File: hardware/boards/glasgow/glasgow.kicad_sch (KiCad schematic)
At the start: 95 parts, among them J1 USB_C_USB2.0, SW1 RST, U1 CY7C68013A-56LTX, U15 TPD3S014, U2 CAT24M01X, U3 BL24C256A-SFRC, U30 ICE40HX8K-BG121, U36 TLV73312PQDRVR, U7 APX811-40UG-7, U8 TLV75533PDRVR, Y1 24M

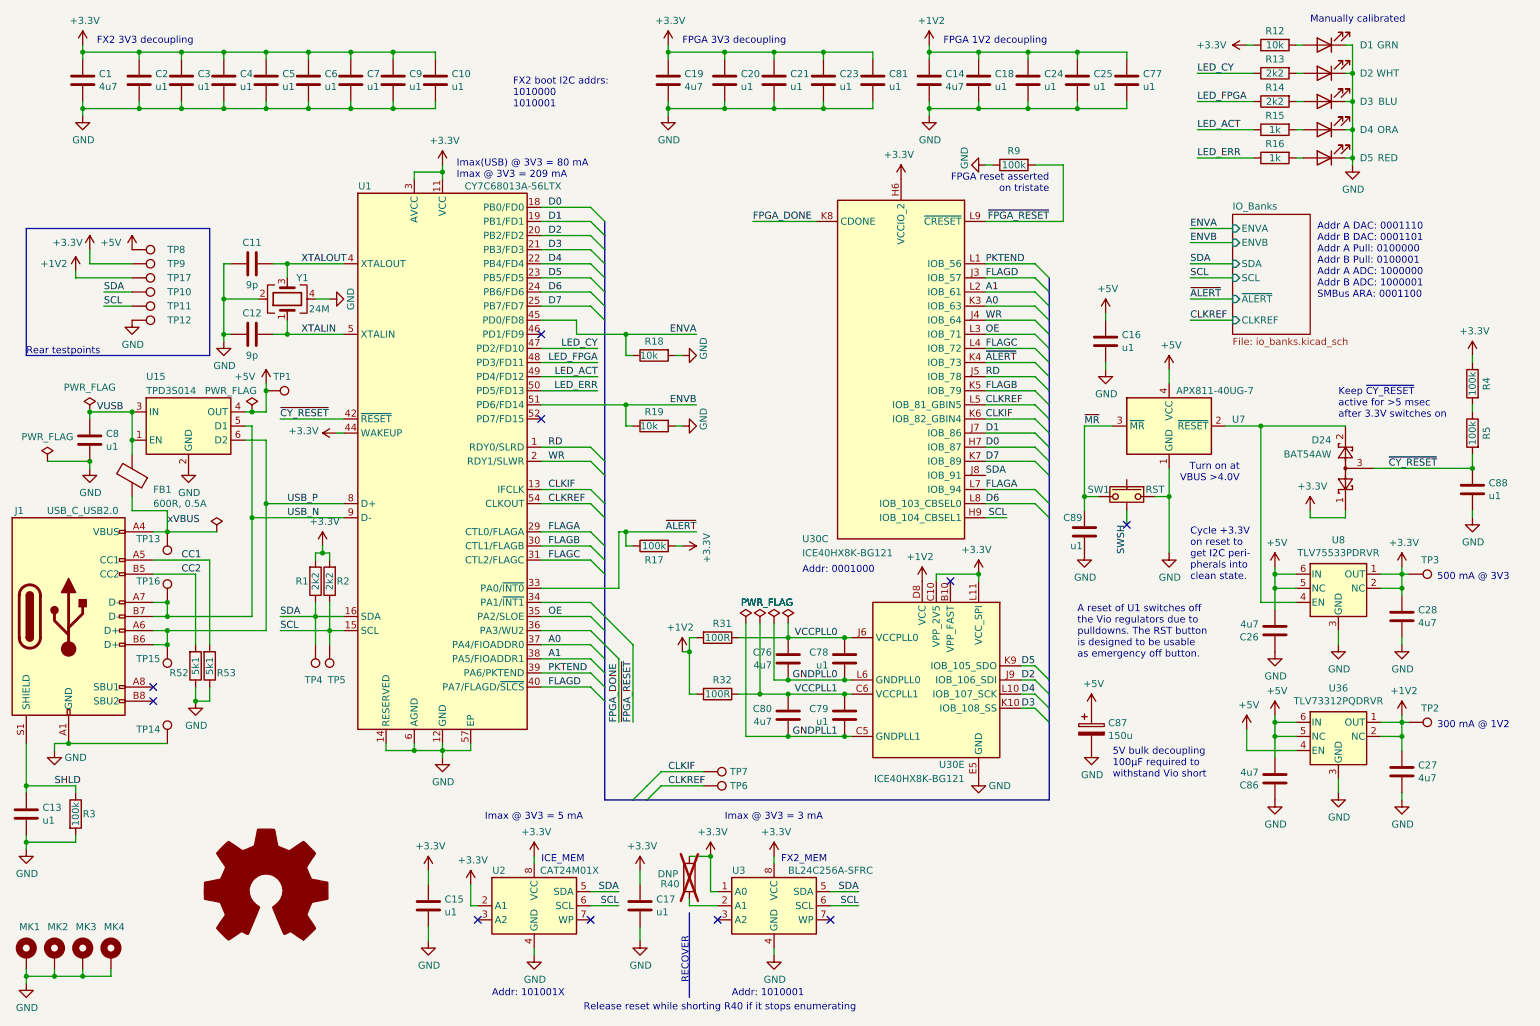
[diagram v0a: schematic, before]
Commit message: JLCPCB part swaps
Switch parts to be either of:
- cheaper
- in stock
- order-able
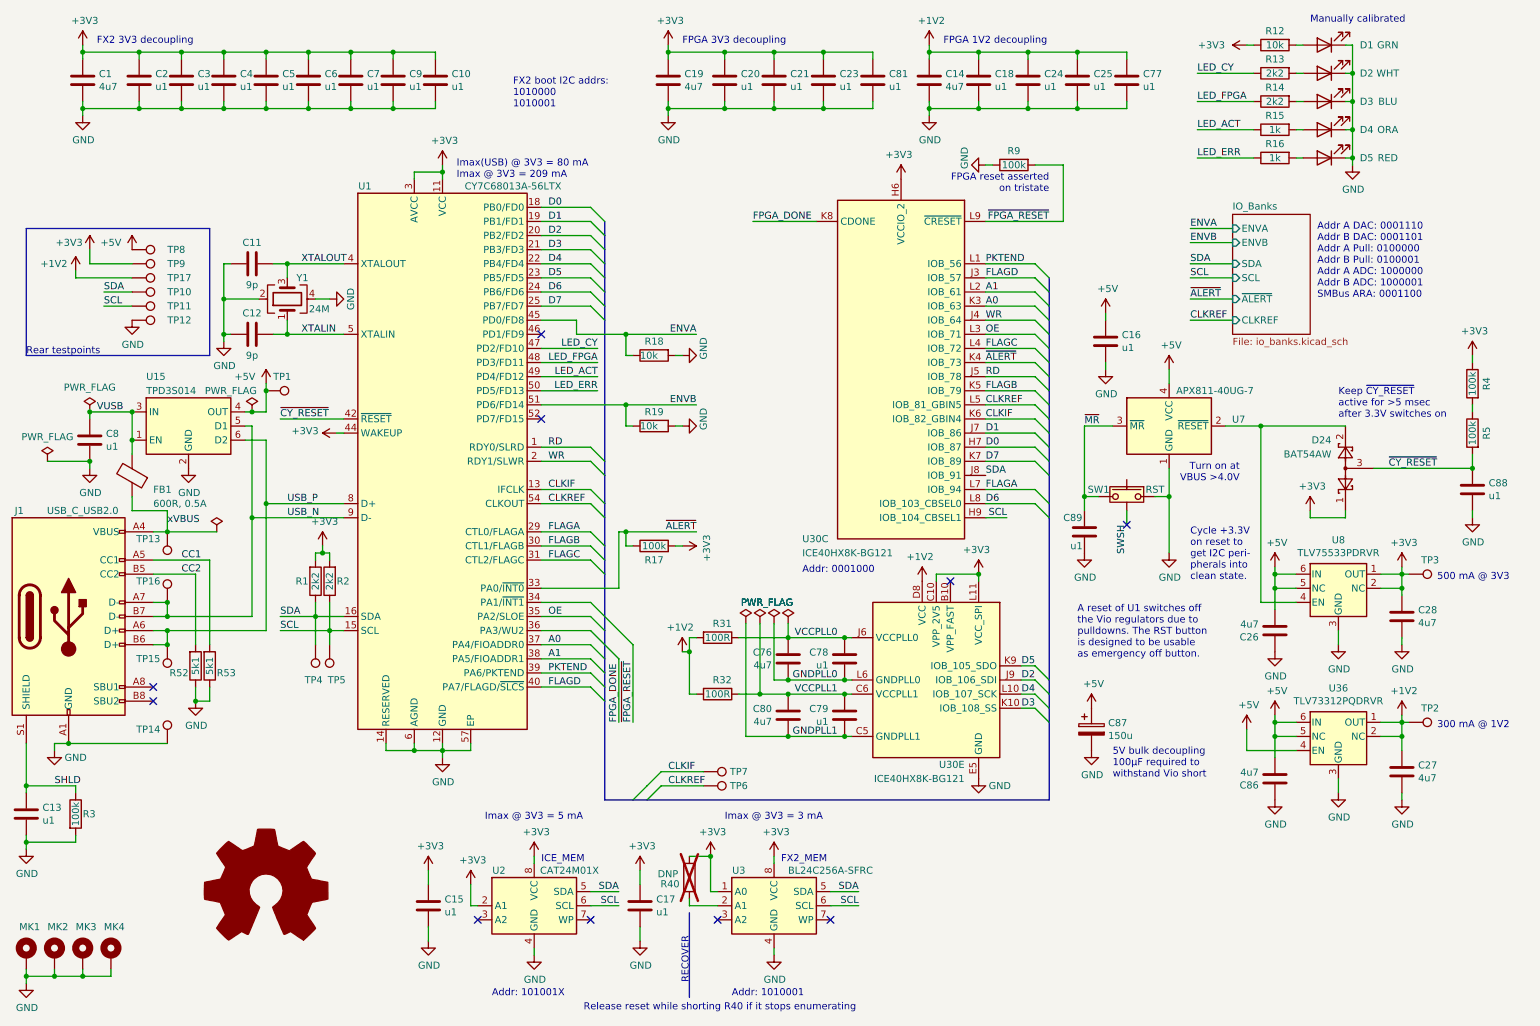
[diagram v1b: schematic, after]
